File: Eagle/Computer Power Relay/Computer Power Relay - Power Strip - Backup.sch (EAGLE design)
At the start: 9 parts, among them K1 RELAY-3V3DC-110VAC012, K2 RELAY-110VACV3_IN-PLACE, K3 RELAY-110VACV3_SMD

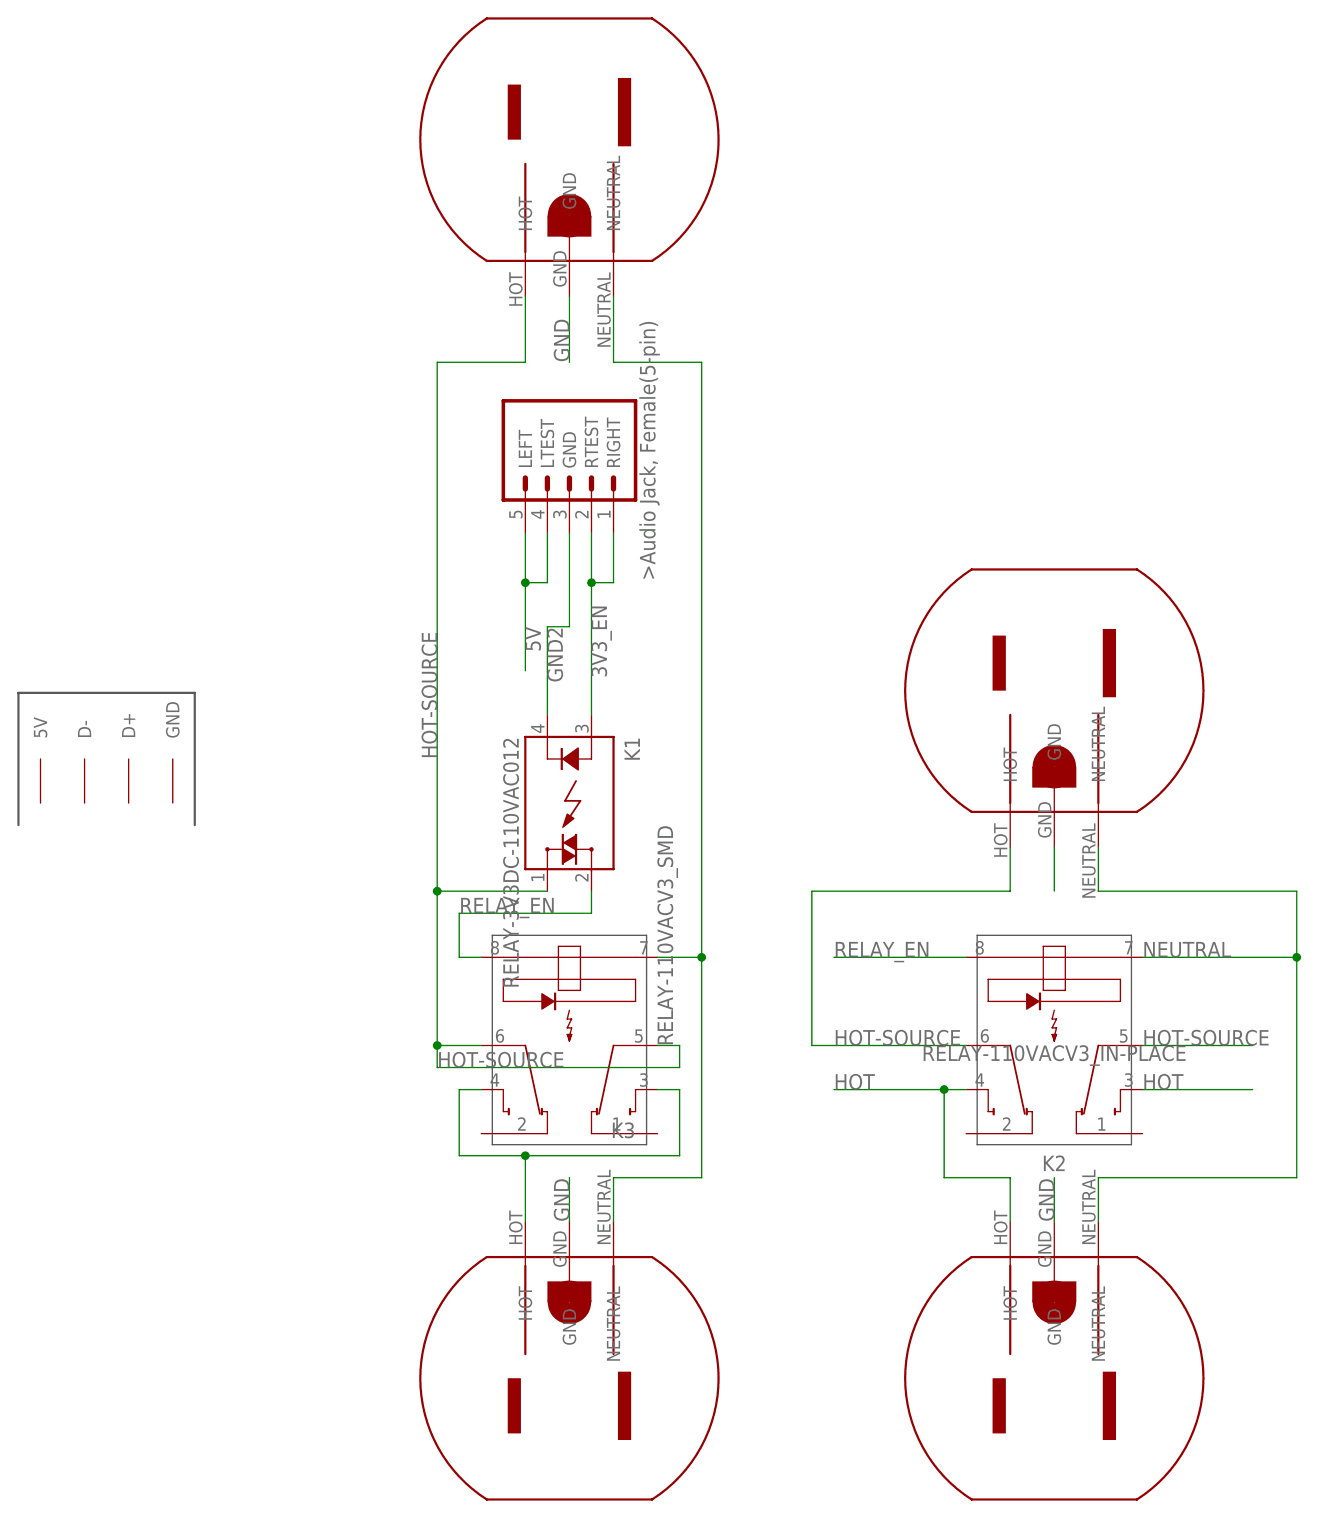
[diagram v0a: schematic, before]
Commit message: Beginning Merge of Boards (Relay)
I'm beginning to merge the Controller and Power Strip boards into one so that I can print it for cheaper.
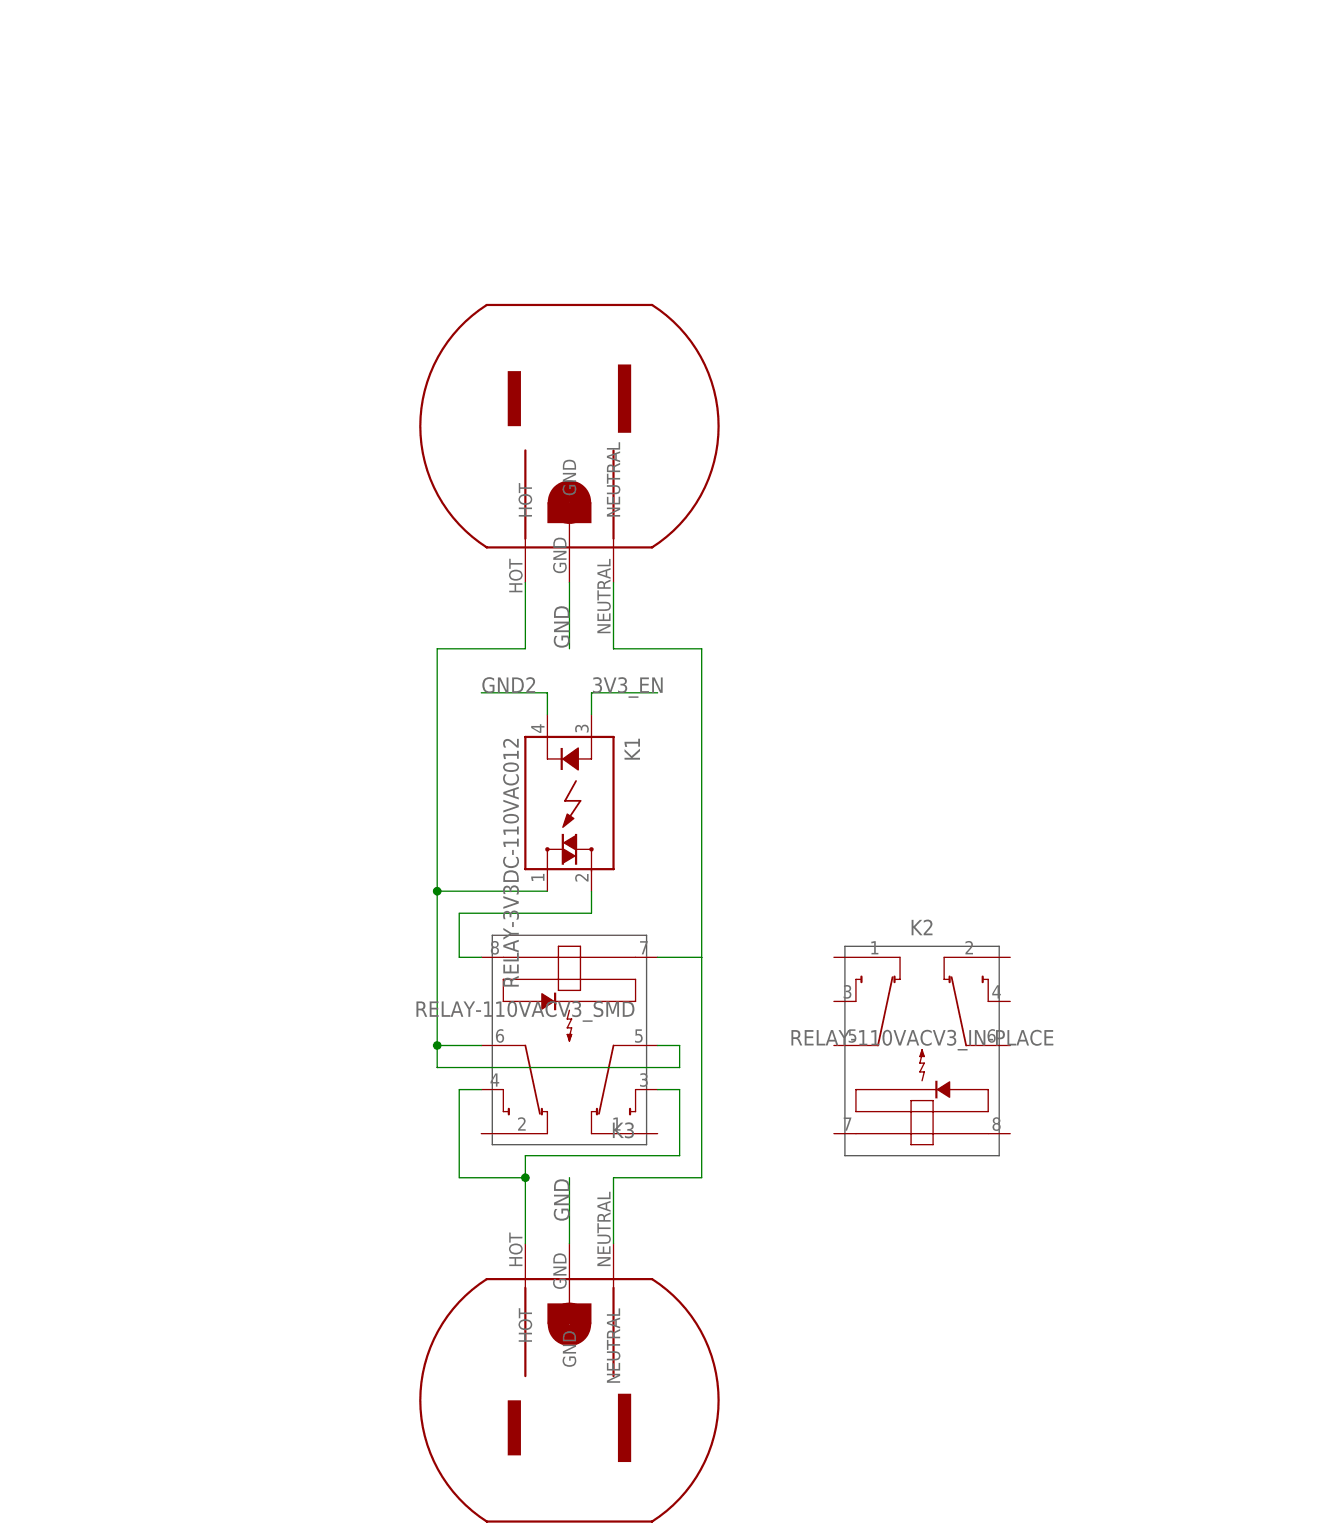
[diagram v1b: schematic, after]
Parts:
- removed U$3: MAINS-POWER-OUTLET3-PIN-SMD, Inventory:MAINS-POWER-OUTLET3-PIN-SMD
- removed U$4, U$5: MAINS-POWER-OUTLET3-PIN, Inventory:MAINS-POWER-OUTLET3-PIN
- removed U$6: PCB_USB, Inventory:PCB_USB
- U$1: value AUDIO_JACK_FEMALE_5-PIN -> MAINS-POWER-OUTLET3-PIN; device Inventory:AUDIO_JACK_FEMALE_5-PIN -> Inventory:MAINS-POWER-OUTLET3-PIN
- U$2: value MAINS-POWER-OUTLET3-PIN-SMD -> MAINS-POWER-OUTLET3-PIN; device Inventory:MAINS-POWER-OUTLET3-PIN-SMD -> Inventory:MAINS-POWER-OUTLET3-PIN
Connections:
- removed net 5V: U$1.LEFT, U$1.LTEST
- removed net HOT: K2.3, K2.4, U$4.HOT
- removed net HOT-SOURCE: K1.1, K2.5, K2.6, K3.5, K3.6, U$3.HOT, U$5.HOT
- removed net N$2: K3.7, U$2.NEUTRAL, U$3.NEUTRAL
- removed net N$3: U$5.GND
- removed net NEUTRAL: K2.7, U$4.NEUTRAL, U$5.NEUTRAL
- removed net RELAY_EN: K1.2, K2.8, K3.8
- new net N$11: K1.1, K3.5, K3.6, U$2.HOT
- new net N$12: K3.7, U$1.NEUTRAL, U$2.NEUTRAL
- new net N$14: K1.2, K3.8
- net 3V3_EN: no longer U$1.RIGHT, U$1.RTEST
- net GND: now also U$1.GND; no longer U$3.GND, U$4.GND
- net GND2: no longer U$1.GND
- net N$1: now also U$1.HOT; no longer U$2.HOT
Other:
- moved on the sheet: K2
